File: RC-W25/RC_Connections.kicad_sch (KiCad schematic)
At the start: 19 parts, among them J1 USB_C_Receptacle_USB2.0_14P, U1 ESP32-C6-WROOM-1

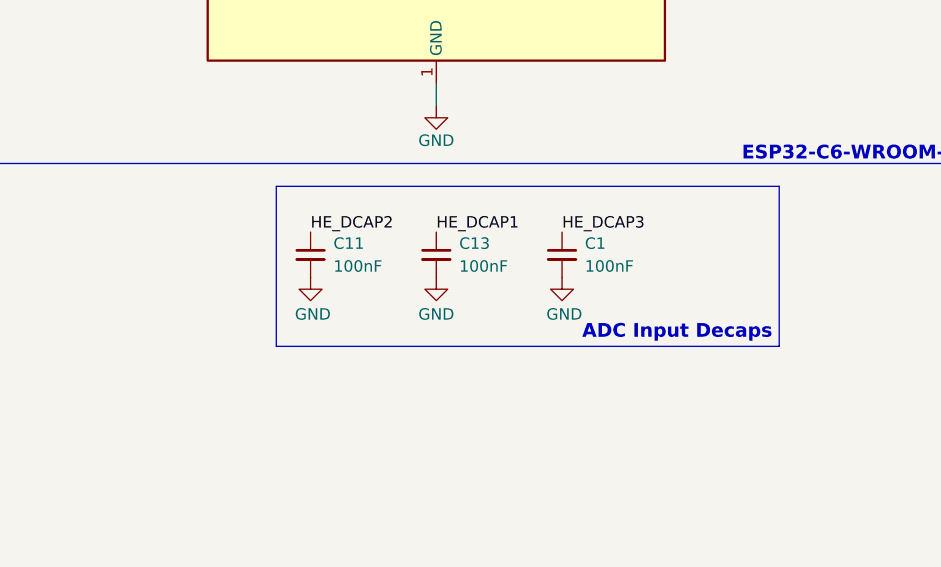
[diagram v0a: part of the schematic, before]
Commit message: Updated Battery
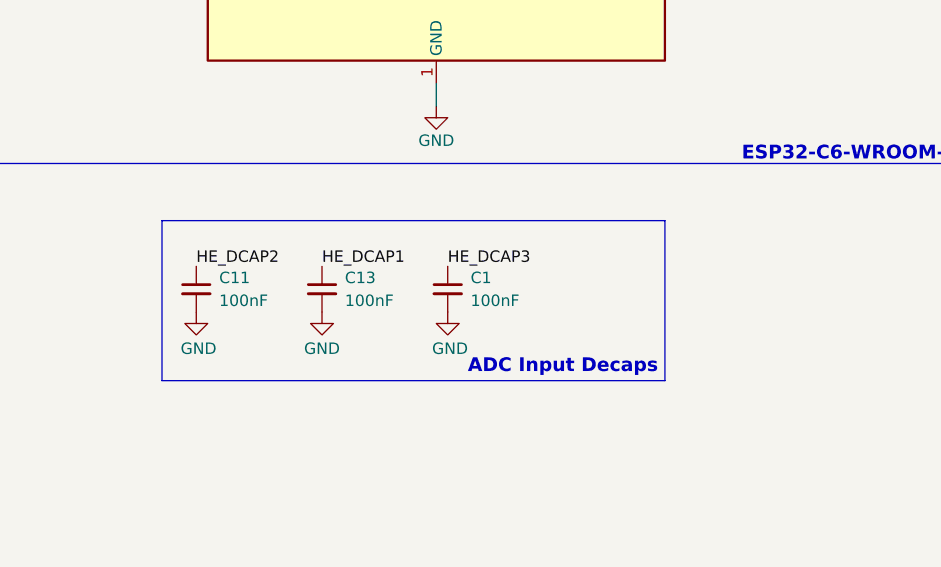
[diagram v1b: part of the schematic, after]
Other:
- moved on the sheet: C1, C11, C13
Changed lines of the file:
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@@
 	)
 	(rectangle
-		(start 175.26 109.22)
-		(end 231.14 127)
+		(start 162.56 113.03)
+		(end 218.44 130.81)
 		(stroke
 			(width 0)
@@
 	(text "ADC Input Decaps"
 		(exclude_from_sim no)
-		(at 230.378 125.476 0)
+		(at 217.678 129.286 0)
 		(effects
 			(font
@@
 	)
 	(label "HE_DCAP3"
-		(at 207.01 114.3 0)
+		(at 194.31 118.11 0)
 		(effects
 			(font
@@
 	)
 	(label "HE_DCAP2"
-		(at 179.07 114.3 0)
+		(at 166.37 118.11 0)
 		(effects
 			(font
@@
 	)
 	(label "HE_DCAP1"
-		(at 193.04 114.3 0)
+		(at 180.34 118.11 0)
 		(effects
 			(font
@@
 	(symbol
 		(lib_id "Device:C_Small")
-		(at 179.07 116.84 0)
+		(at 166.37 120.65 0)
 		(unit 1)
 		(exclude_from_sim no)
@@
 		(fields_autoplaced yes)
 		(property "Reference" "C11"
-			(at 181.61 115.5762 0)
+			(at 168.91 119.3862 0)
 			(effects
 				(font
@@
 		)
 		(property "Value" "100nF"
-			(at 181.61 118.1162 0)
+			(at 168.91 121.9262 0)
 			(effects
 				(font
@@
 		)
 		(property "Footprint" "Capacitor_SMD:C_0603_1608Metric"
-			(at 179.07 116.84 0)
+			(at 166.37 120.65 0)
 			(effects
 				(font
@@
 		)
 		(property "Datasheet" "~"
-			(at 179.07 116.84 0)
+			(at 166.37 120.65 0)
 			(effects
 				(font
@@
 		)
 		(property "Description" "Unpolarized capacitor, small symbol"
-			(at 179.07 116.84 0)
+			(at 166.37 120.65 0)
 			(effects
 				(font
@@
 	(symbol
 		(lib_id "power:GND")
-		(at 207.01 119.38 0)
+		(at 194.31 123.19 0)
 		(unit 1)
 		(exclude_from_sim no)
@@
 		(dnp no)
 		(property "Reference" "#PWR04"
-			(at 207.01 125.73 0)
+			(at 194.31 129.54 0)
 			(effects
 				(font
@@
 		)
 		(property "Value" "GND"
-			(at 207.264 123.444 0)
+			(at 194.564 127.254 0)
 			(effects
 				(font
@@
 		)
 		(property "Footprint" ""
-			(at 207.01 119.38 0)
+			(at 194.31 123.19 0)
 			(effects
 				(font
@@
 		)
 		(property "Datasheet" ""
-			(at 207.01 119.38 0)
+			(at 194.31 123.19 0)
 			(effects
 				(font
@@
 		)
 		(property "Description" "Power symbol creates a global label with name \"GND\" , ground"
-			(at 207.01 119.38 0)
+			(at 194.31 123.19 0)
 			(effects
 				(font
@@
 	(symbol
 		(lib_id "power:GND")
-		(at 193.04 119.38 0)
+		(at 180.34 123.19 0)
 		(unit 1)
 		(exclude_from_sim no)
@@
 		(dnp no)
 		(property "Reference" "#PWR026"
-			(at 193.04 125.73 0)
+			(at 180.34 129.54 0)
 			(effects
 				(font
@@
 		)
 		(property "Value" "GND"
-			(at 193.04 123.444 0)
+			(at 180.34 127.254 0)
 			(effects
 				(font
@@
 		)
 		(property "Footprint" ""
-			(at 193.04 119.38 0)
+			(at 180.34 123.19 0)
 			(effects
 				(font
@@
 		)
 		(property "Datasheet" ""
-			(at 193.04 119.38 0)
+			(at 180.34 123.19 0)
 			(effects
 				(font
@@
 		)
 		(property "Description" "Power symbol creates a global label with name \"GND\" , ground"
-			(at 193.04 119.38 0)
+			(at 180.34 123.19 0)
 			(effects
 				(font
@@
 	(symbol
 		(lib_id "Device:C_Small")
-		(at 193.04 116.84 0)
+		(at 180.34 120.65 0)
 		(unit 1)
 		(exclude_from_sim no)
@@
 		(fields_autoplaced yes)
 		(property "Reference" "C13"
-			(at 195.58 115.5762 0)
+			(at 182.88 119.3862 0)
 			(effects
 				(font
@@
 		)
 		(property "Value" "100nF"
-			(at 195.58 118.1162 0)
+			(at 182.88 121.9262 0)
 			(effects
 				(font
@@
 		)
 		(property "Footprint" "Capacitor_SMD:C_0603_1608Metric"
-			(at 193.04 116.84 0)
+			(at 180.34 120.65 0)
 			(effects
 				(font
@@
 		)
 		(property "Datasheet" "~"
-			(at 193.04 116.84 0)
+			(at 180.34 120.65 0)
 			(effects
 				(font
@@
 		)
 		(property "Description" "Unpolarized capacitor, small symbol"
-			(at 193.04 116.84 0)
+			(at 180.34 120.65 0)
 			(effects
 				(font
@@
 	(symbol
 		(lib_id "power:GND")
-		(at 179.07 119.38 0)
+		(at 166.37 123.19 0)
 		(unit 1)
 		(exclude_from_sim no)
@@
 		(dnp no)
 		(property "Reference" "#PWR025"
-			(at 179.07 125.73 0)
+			(at 166.37 129.54 0)
 			(effects
 				(font
@@
 		)
 		(property "Value" "GND"
-			(at 179.324 123.444 0)
+			(at 166.624 127.254 0)
 			(effects
 				(font
@@
 		)
 		(property "Footprint" ""
-			(at 179.07 119.38 0)
+			(at 166.37 123.19 0)
 			(effects
 				(font
@@
 		)
 		(property "Datasheet" ""
-			(at 179.07 119.38 0)
+			(at 166.37 123.19 0)
 			(effects
 				(font
@@
 		)
 		(property "Description" "Power symbol creates a global label with name \"GND\" , ground"
-			(at 179.07 119.38 0)
+			(at 166.37 123.19 0)
 			(effects
 				(font
@@
 	(symbol
 		(lib_id "Device:C_Small")
-		(at 207.01 116.84 0)
+		(at 194.31 120.65 0)
 		(unit 1)
 		(exclude_from_sim no)
@@
 		(fields_autoplaced yes)
 		(property "Reference" "C1"
-			(at 209.55 115.5762 0)
+			(at 196.85 119.3862 0)
 			(effects
 				(font
@@
 		)
 		(property "Value" "100nF"
-			(at 209.55 118.1162 0)
+			(at 196.85 121.9262 0)
 			(effects
 				(font
@@
 		)
 		(property "Footprint" "Capacitor_SMD:C_0603_1608Metric"
-			(at 207.01 116.84 0)
+			(at 194.31 120.65 0)
 			(effects
 				(font
@@
 		)
 		(property "Datasheet" "~"
-			(at 207.01 116.84 0)
+			(at 194.31 120.65 0)
 			(effects
 				(font
@@
 		)
 		(property "Description" "Unpolarized capacitor, small symbol"
-			(at 207.01 116.84 0)
-			(effects
-				(font
+			(at 194.31 120.65 0)
+			(effects
+				(font

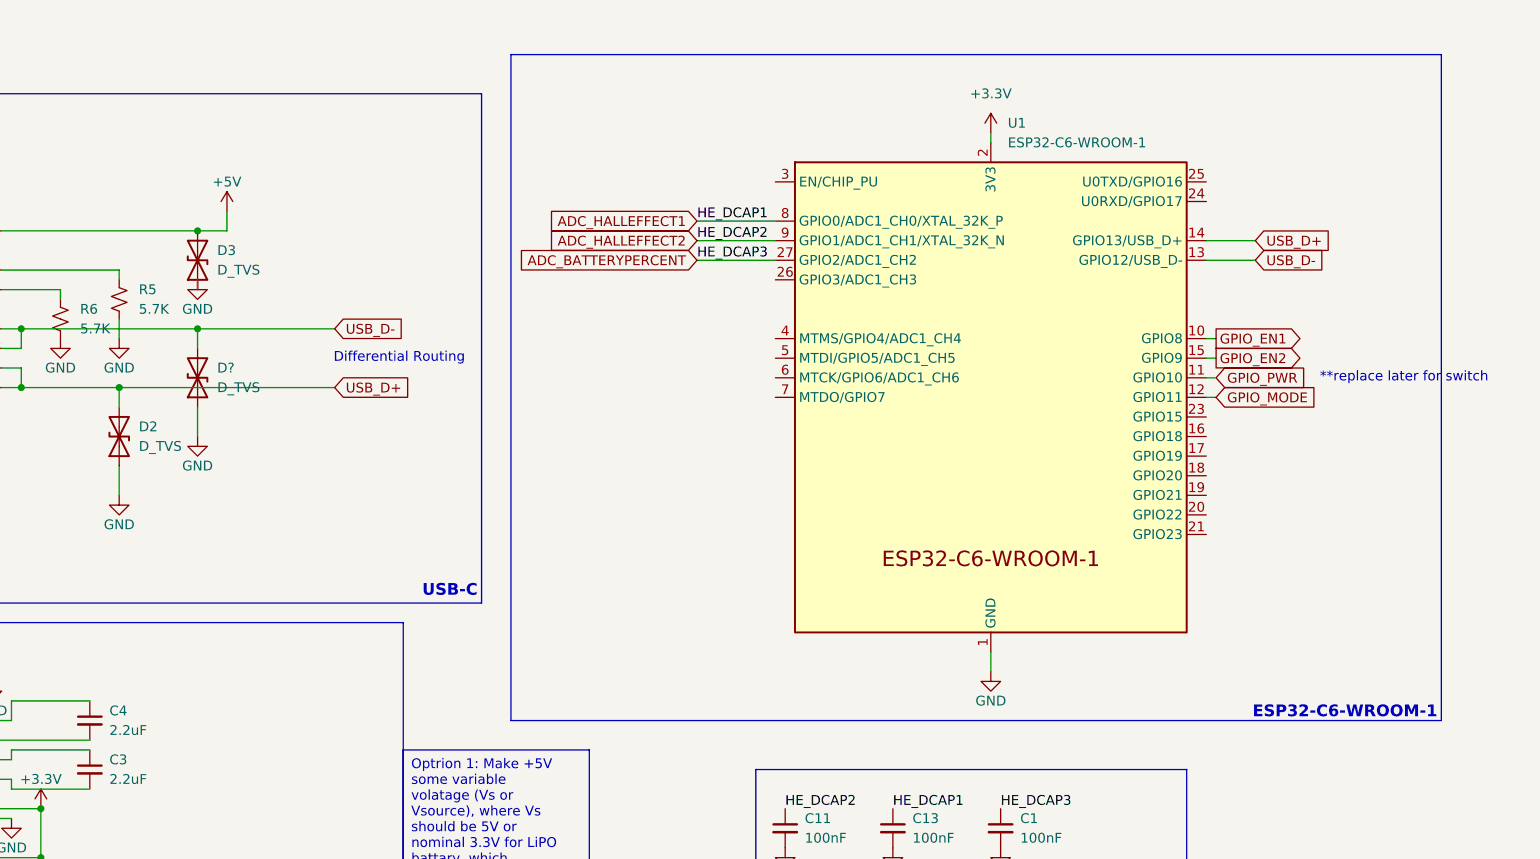
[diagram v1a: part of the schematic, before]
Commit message: Updated Footprints
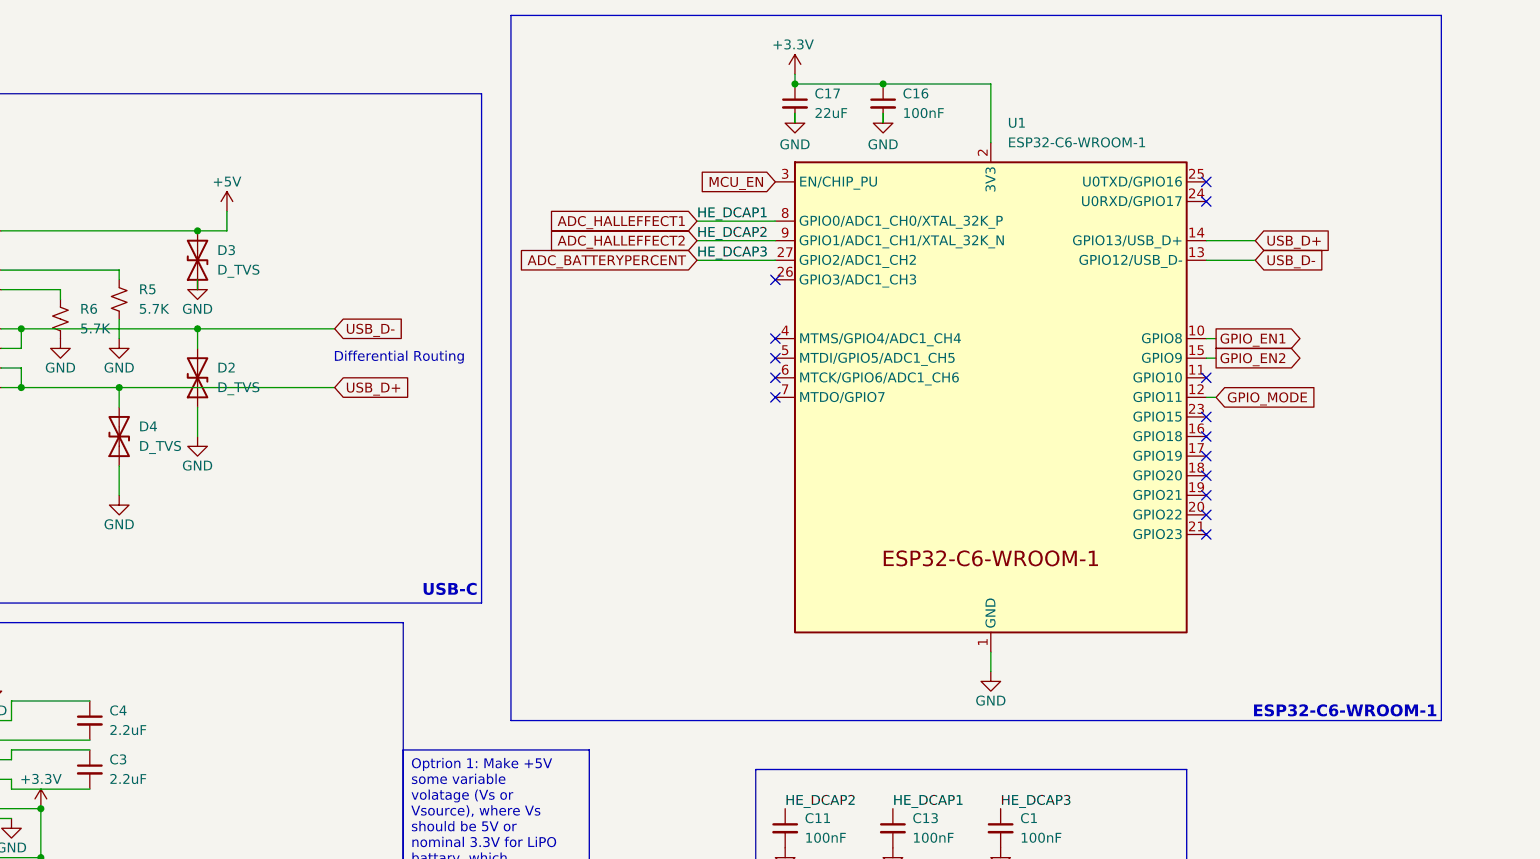
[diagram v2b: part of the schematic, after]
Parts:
- removed D?: D_TVS, symbol Device:D_TVS
- added C16: 100nF, Capacitor_SMD:C_0603_1608Metric, symbol Device:C_Small
- added C17: 22uF, Capacitor_SMD:C_0603_1608Metric, symbol Device:C_Small
- added D4: D_TVS, Diode_SMD:D_0603_1608Metric, symbol Device:D_TVS
- D2, D3: footprint (none) -> Diode_SMD:D_0603_1608Metric
- J1: footprint (none) -> Connector_USB:USB_C_Receptacle_GCT_USB4105-xx-A_16P_TopMnt_Horizontal
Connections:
- net +3.3V: now also C16.1, C17.1
- net GND: now also C16.2, C17.2, D4.1 (A1)
- net USB_D+: now also D4.2 (A2); no longer D2.2 (A2)
- net USB_D-: now also D2.2 (A2)
- net MCU_EN: now reaches U1.3 (EN/CHIP_PU)
- net GPIO_PWR: no longer names the net of U1.11 (GPIO10)
- no-connect marks 1 -> 16
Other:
- note removed: "**replace later for switch"

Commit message: Almost Finalized Schematic
Still need to spec out buttons and jst conn
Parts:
- removed C1: 100nF, Capacitor_SMD:C_0603_1608Metric, symbol Device:C_Small
- added C19: 1uF, Capacitor_SMD:C_0805_2012Metric, symbol Device:C_Small
- added C9: 100nF, Capacitor_SMD:C_0402_1005Metric, symbol Device:C_Small
- added R16, R7: 10k, Resistor_SMD:R_0402_1005Metric, symbol Device:R_Small_US
- added SW3, SW4: Button, symbol Switch:SW_Push
- C1: renamed from C?; footprint Capacitor_SMD:C_0603_1608Metric -> Capacitor_SMD:C_0402_1005Metric; LCSC# (none) -> C338067
- C2: footprint Capacitor_SMD:C_0603_1608Metric -> Capacitor_SMD:C_0402_1005Metric; LCSC# (none) -> C338067
- C3: renamed from C4; footprint Capacitor_SMD:C_0603_1608Metric -> Capacitor_SMD:C_0402_1005Metric; LCSC# (none) -> C338067
- C4: renamed from C3; footprint Capacitor_SMD:C_0603_1608Metric -> Capacitor_SMD:C_0402_1005Metric; LCSC# (none) -> C338067
- C5: renamed from C11; footprint Capacitor_SMD:C_0603_1608Metric -> Capacitor_SMD:C_0402_1005Metric; LCSC# (none) -> C22435938
- C6: renamed from C17; footprint Capacitor_SMD:C_0603_1608Metric -> Capacitor_SMD:C_0805_2012Metric; LCSC# (none) -> C380337
- C7: renamed from C16; footprint Capacitor_SMD:C_0603_1608Metric -> Capacitor_SMD:C_0402_1005Metric; LCSC# (none) -> C22435938
- C8: renamed from C13; footprint Capacitor_SMD:C_0603_1608Metric -> Capacitor_SMD:C_0402_1005Metric; LCSC# (none) -> C22435938
- D1: renamed from D4; value D_TVS -> 6V TVS; footprint Diode_SMD:D_0603_1608Metric -> Diode_SMD:D_0402_1005Metric; LCSC# (none) -> C316043
- D2: renamed from D3; value D_TVS -> 6V TVS; footprint Diode_SMD:D_0603_1608Metric -> Diode_SMD:D_0402_1005Metric; LCSC# (none) -> C316043
- D3: renamed from D2; value D_TVS -> 6V TVS; footprint Diode_SMD:D_0603_1608Metric -> Diode_SMD:D_0402_1005Metric; LCSC# (none) -> C316043
- DS1: value ~ -> FPC 0.5mm 30P
- J1: LCSC# (none) -> C165948
- R1: renamed from R4; value 4.7K -> 4.7k; footprint Resistor_SMD:R_0603_1608Metric -> Resistor_SMD:R_0402_1005Metric; LCSC# (none) -> C317921
- R2: renamed from R6; value 5.7K -> 5.7k; footprint Resistor_SMD:R_0603_1608Metric -> Resistor_SMD:R_0402_1005Metric; LCSC# (none) -> C852861
- R3: value 4.7K -> 4.7k; footprint Resistor_SMD:R_0603_1608Metric -> Resistor_SMD:R_0402_1005Metric; LCSC# (none) -> C317921
- R4: renamed from R5; value 5.7K -> 5.7k; footprint Resistor_SMD:R_0603_1608Metric -> Resistor_SMD:R_0402_1005Metric; LCSC# (none) -> C852861
- R5: renamed from R?; LCSC# (none) -> C861364
- R6: renamed from R2; value 4.7K -> 4.7k; footprint Resistor_SMD:R_0603_1608Metric -> Resistor_SMD:R_0402_1005Metric; LCSC# (none) -> C317921
- U1: LCSC# (none) -> C5736265
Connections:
- net +3.3V: now also R16.1, R7.1
- net ADC_BATTERYPERCENT: now also C9.1
- net ADC_HALLEFFECT1: now also C5.1; no longer C8.1
- net ADC_HALLEFFECT2: now also C8.1; no longer C5.1
- net GND: now also C19.2, C9.2, SW3.2, SW4.2
- net GPIO_EN1: now also U1.23 (GPIO15); no longer U1.10 (GPIO8)
- net GPIO_EN2: now also U1.16 (GPIO18); no longer U1.15 (GPIO9)
- net +5V renamed +USB5V
- net MCU_EN renamed RESET
- net RESET: now also C19.1, R7.2, SW3.1
- new net: R16.2, U1.10 (GPIO8)
- new net FLASH: SW4.1, U1.15 (GPIO9)
- no-connect marks 16 -> 14
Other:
- moved on the sheet: C5
